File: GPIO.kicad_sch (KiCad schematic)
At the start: 10 parts

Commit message: PCB drawn
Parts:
- C30, C31: value (none) -> 100n; footprint (none) -> Capacitor_SMD:C_0603_1608Metric
- R15: value (none) -> 10K; footprint (none) -> Resistor_SMD:R_0603_1608Metric
- R16, R17: value (none) -> 4.7K; footprint (none) -> Resistor_SMD:R_0603_1608Metric
- R18: value (none) -> 2.2K; footprint (none) -> Resistor_SMD:R_0603_1608Metric
- R19, R20: value (none) -> 68; footprint (none) -> Resistor_SMD:R_0603_1608Metric
- U10: value (none) -> PCF8574; footprint (none) -> EXTRA IC:SOIC127P1032X265-16N
- U9: value (none) -> ATtiny85V-10S; footprint (none) -> Package_SO:SOIC-8W_5.3x5.3mm_P1.27mm
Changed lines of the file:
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@@
   (symbol (lib_id "power:GND") (at 168.91 107.95 0) (unit 1)
     (in_bom yes) (on_board yes) (fields_autoplaced)
-    (property "Reference" "#PWR?" (id 0) (at 168.91 114.3 0)
-      (effects (font (size 1.27 1.27)) hide)
-    )
-    (property "Value" "" (id 1) (at 168.91 112.3934 0))
+    (property "Reference" "#PWR0124" (id 0) (at 168.91 114.3 0)
+      (effects (font (size 1.27 1.27)) hide)
+    )
+    (property "Value" "GND" (id 1) (at 168.91 112.3934 0))
     (property "Footprint" "" (id 2) (at 168.91 107.95 0)
       (effects (font (size 1.27 1.27)) hide)
@@
   (symbol (lib_id "power:GND") (at 182.88 124.46 0) (unit 1)
     (in_bom yes) (on_board yes) (fields_autoplaced)
-    (property "Reference" "#PWR?" (id 0) (at 182.88 130.81 0)
-      (effects (font (size 1.27 1.27)) hide)
-    )
-    (property "Value" "" (id 1) (at 182.88 128.9034 0))
+    (property "Reference" "#PWR0120" (id 0) (at 182.88 130.81 0)
+      (effects (font (size 1.27 1.27)) hide)
+    )
+    (property "Value" "GND" (id 1) (at 182.88 128.9034 0))
     (property "Footprint" "" (id 2) (at 182.88 124.46 0)
       (effects (font (size 1.27 1.27)) hide)
@@
   (symbol (lib_id "power:GND") (at 110.49 120.65 0) (unit 1)
     (in_bom yes) (on_board yes) (fields_autoplaced)
-    (property "Reference" "#PWR?" (id 0) (at 110.49 127 0)
-      (effects (font (size 1.27 1.27)) hide)
-    )
-    (property "Value" "" (id 1) (at 110.49 125.0934 0))
+    (property "Reference" "#PWR0121" (id 0) (at 110.49 127 0)
+      (effects (font (size 1.27 1.27)) hide)
+    )
+    (property "Value" "GND" (id 1) (at 110.49 125.0934 0))
     (property "Footprint" "" (id 2) (at 110.49 120.65 0)
       (effects (font (size 1.27 1.27)) hide)
@@
       (effects (font (size 1.27 1.27)) (justify right))
     )
-    (property "Value" "" (id 1) (at 153.8986 89.3322 0)
-      (effects (font (size 1.27 1.27)) (justify right))
-    )
-    (property "Footprint" "" (id 2) (at 152.4 87.63 0)
+    (property "Value" "10K" (id 1) (at 153.8986 89.3322 0)
+      (effects (font (size 1.27 1.27)) (justify right))
+    )
+    (property "Footprint" "Resistor_SMD:R_0603_1608Metric" (id 2) (at 152.4 87.63 0)
       (effects (font (size 1.27 1.27)) hide)
     )
@@
     (in_bom yes) (on_board yes)
     (property "Reference" "R19" (id 0) (at 133.35 101.6 90))
-    (property "Value" "" (id 1) (at 130.81 100.33 90))
-    (property "Footprint" "" (id 2) (at 130.81 102.87 0)
+    (property "Value" "68" (id 1) (at 130.81 100.33 90))
+    (property "Footprint" "Resistor_SMD:R_0603_1608Metric" (id 2) (at 130.81 102.87 0)
       (effects (font (size 1.27 1.27)) hide)
     )
@@
       (effects (font (size 1.27 1.27)) (justify left))
     )
-    (property "Value" "" (id 1) (at 184.8994 87.7371 0)
-      (effects (font (size 1.27 1.27)) (justify left))
-    )
-    (property "Footprint" "" (id 2) (at 182.88 104.14 0)
+    (property "Value" "PCF8574" (id 1) (at 184.8994 87.7371 0)
+      (effects (font (size 1.27 1.27)) (justify left))
+    )
+    (property "Footprint" "EXTRA IC:SOIC127P1032X265-16N" (id 2) (at 182.88 104.14 0)
       (effects (font (size 1.27 1.27)) hide)
     )
@@
     (in_bom yes) (on_board yes)
     (property "Reference" "R20" (id 0) (at 133.35 104.14 90))
-    (property "Value" "" (id 1) (at 130.81 107.95 90))
-    (property "Footprint" "" (id 2) (at 130.81 105.41 0)
+    (property "Value" "68" (id 1) (at 130.81 107.95 90))
+    (property "Footprint" "Resistor_SMD:R_0603_1608Metric" (id 2) (at 130.81 105.41 0)
       (effects (font (size 1.27 1.27)) hide)
     )
@@
   (symbol (lib_id "power:GND") (at 64.77 101.6 0) (unit 1)
     (in_bom yes) (on_board yes) (fields_autoplaced)
-    (property "Reference" "#PWR?" (id 0) (at 64.77 107.95 0)
-      (effects (font (size 1.27 1.27)) hide)
-    )
-    (property "Value" "" (id 1) (at 64.77 106.0434 0))
+    (property "Reference" "#PWR0122" (id 0) (at 64.77 107.95 0)
+      (effects (font (size 1.27 1.27)) hide)
+    )
+    (property "Value" "GND" (id 1) (at 64.77 106.0434 0))
     (property "Footprint" "" (id 2) (at 64.77 101.6 0)
       (effects (font (size 1.27 1.27)) hide)
@@
       (effects (font (size 1.27 1.27)) (justify right))
     )
-    (property "Value" "" (id 1) (at 138.6586 96.9522 0)
-      (effects (font (size 1.27 1.27)) (justify right))
-    )
-    (property "Footprint" "" (id 2) (at 137.16 95.25 0)
+    (property "Value" "2.2K" (id 1) (at 138.6586 96.9522 0)
+      (effects (font (size 1.27 1.27)) (justify right))
+    )
+    (property "Footprint" "Resistor_SMD:R_0603_1608Metric" (id 2) (at 137.16 95.25 0)
       (effects (font (size 1.27 1.27)) hide)
     )
@@
   (symbol (lib_id "power:GND") (at 73.66 101.6 0) (unit 1)
     (in_bom yes) (on_board yes) (fields_autoplaced)
-    (property "Reference" "#PWR?" (id 0) (at 73.66 107.95 0)
-      (effects (font (size 1.27 1.27)) hide)
-    )
-    (property "Value" "" (id 1) (at 73.66 106.0434 0))
+    (property "Reference" "#PWR0123" (id 0) (at 73.66 107.95 0)
+      (effects (font (size 1.27 1.27)) hide)
+    )
+    (property "Value" "GND" (id 1) (at 73.66 106.0434 0))
     (property "Footprint" "" (id 2) (at 73.66 101.6 0)
       (effects (font (size 1.27 1.27)) hide)
@@
       (effects (font (size 1.27 1.27)) (justify right))
     )
-    (property "Value" "" (id 1) (at 97.0281 104.5722 0)
-      (effects (font (size 1.27 1.27)) (justify right))
-    )
-    (property "Footprint" "" (id 2) (at 110.49 102.87 0)
+    (property "Value" "ATtiny85V-10S" (id 1) (at 97.0281 104.5722 0)
+      (effects (font (size 1.27 1.27)) (justify right))
+    )
+    (property "Footprint" "Package_SO:SOIC-8W_5.3x5.3mm_P1.27mm" (id 2) (at 110.49 102.87 0)
       (effects (font (size 1.27 1.27) italic) hide)
     )
@@
       (effects (font (size 1.27 1.27)) (justify left))
     )
-    (property "Value" "" (id 1) (at 75.9841 98.2285 0)
-      (effects (font (size 1.27 1.27)) (justify left))
-    )
-    (property "Footprint" "" (id 2) (at 73.66 96.52 0)
+    (property "Value" "100n" (id 1) (at 75.9841 98.2285 0)
+      (effects (font (size 1.27 1.27)) (justify left))
+    )
+    (property "Footprint" "Capacitor_SMD:C_0603_1608Metric" (id 2) (at 73.66 96.52 0)
       (effects (font (size 1.27 1.27)) hide)
     )
@@
       (effects (font (size 1.27 1.27)) (justify right))
     )
-    (property "Value" "" (id 1) (at 160.2486 89.3322 0)
-      (effects (font (size 1.27 1.27)) (justify right))
-    )
-    (property "Footprint" "" (id 2) (at 158.75 87.63 0)
+    (property "Value" "4.7K" (id 1) (at 160.2486 89.3322 0)
+      (effects (font (size 1.27 1.27)) (justify right))
+    )
+    (property "Footprint" "Resistor_SMD:R_0603_1608Metric" (id 2) (at 158.75 87.63 0)
       (effects (font (size 1.27 1.27)) hide)
     )
@@
       (effects (font (size 1.27 1.27)) (justify right))
     )
-    (property "Value" "" (id 1) (at 167.8686 89.3322 0)
-      (effects (font (size 1.27 1.27)) (justify right))
-    )
-    (property "Footprint" "" (id 2) (at 166.37 87.63 0)
+    (property "Value" "4.7K" (id 1) (at 167.8686 89.3322 0)
+      (effects (font (size 1.27 1.27)) (justify right))
+    )
+    (property "Footprint" "Resistor_SMD:R_0603_1608Metric" (id 2) (at 166.37 87.63 0)
       (effects (font (size 1.27 1.27)) hide)
     )
@@
       (effects (font (size 1.27 1.27)) (justify left))
     )
-    (property "Value" "" (id 1) (at 67.0941 98.2285 0)
-      (effects (font (size 1.27 1.27)) (justify left))
-    )
-    (property "Footprint" "" (id 2) (at 64.77 96.52 0)
-      (effects (font (size 1.27 1.27)) hide)
-    )
+    (property "Value" "100n" (id 1) (at 67.0941 98.2285 0)
+      (effects (font (size 1.27 1.27)) (justify left))
+    )
+    (property "Footprint" "Capacitor_SMD:C_0603_1608Metric" (id 2) (at 64.77 96.52 0)
+      (effects (font (size 1.27 1.27)) hide)
+    )

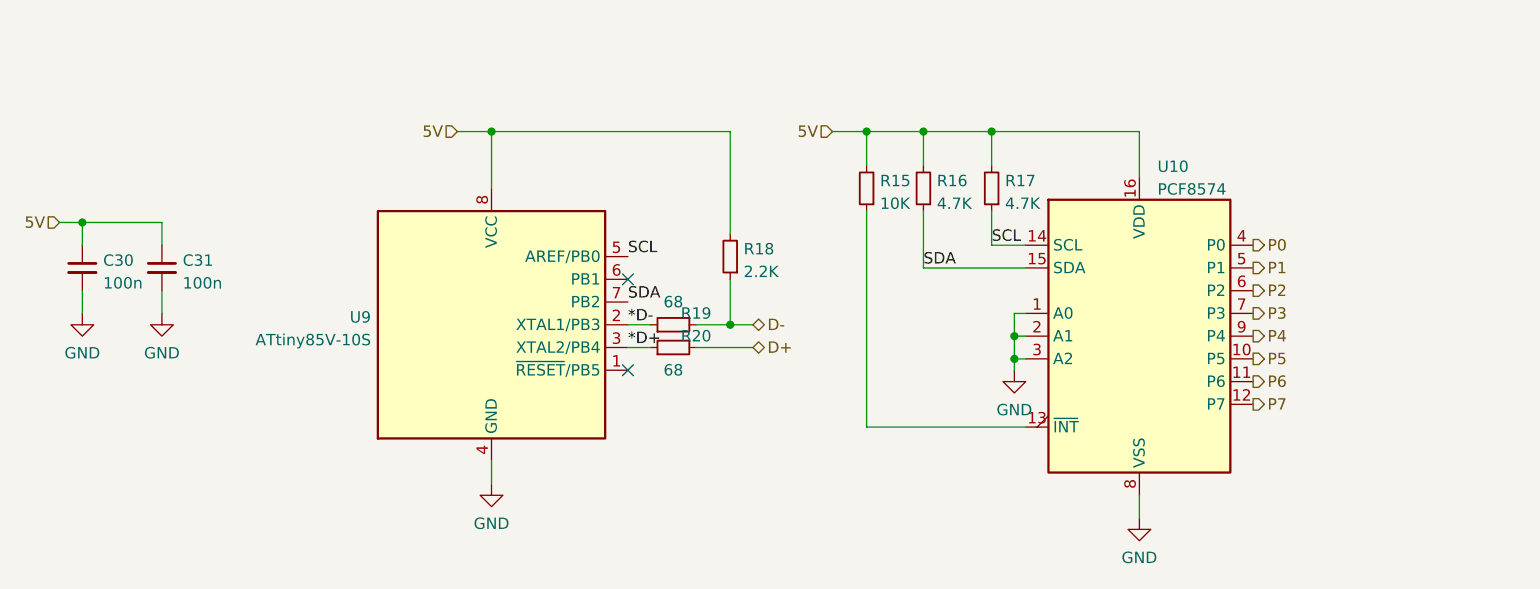
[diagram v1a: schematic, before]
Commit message: Change the map and rebuild the PCB
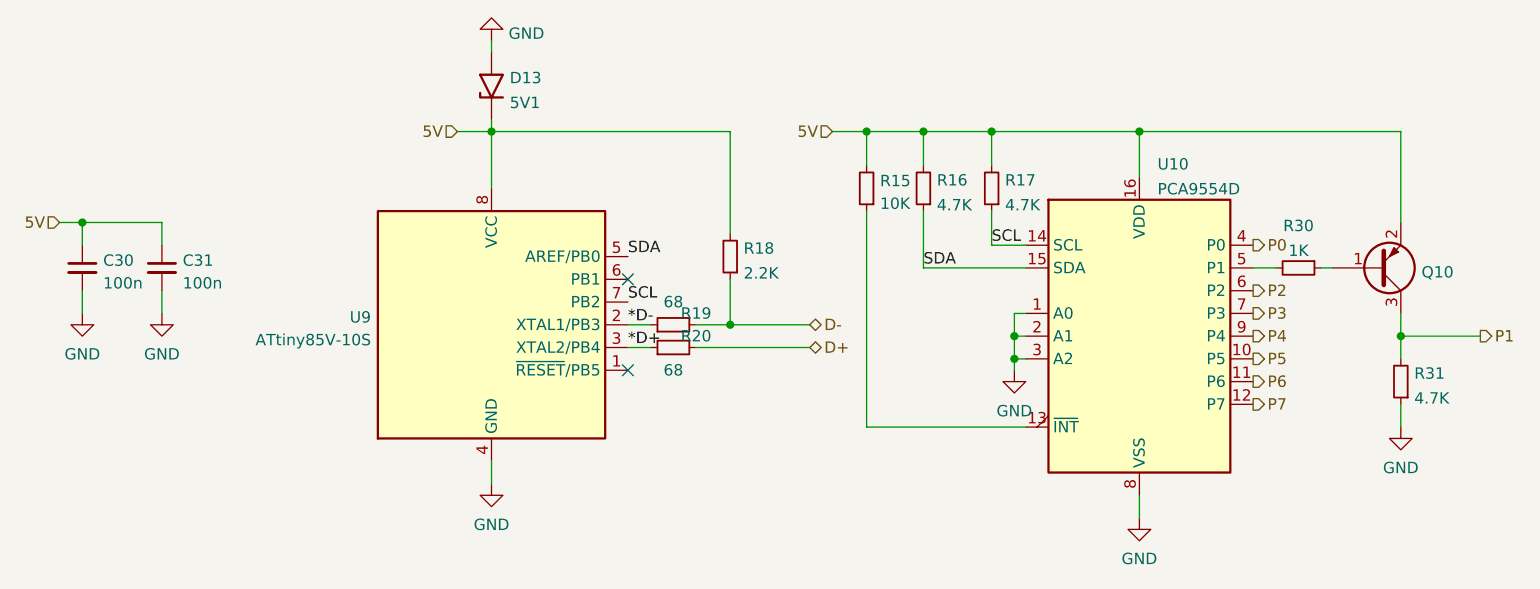
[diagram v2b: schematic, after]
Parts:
- added D13: 5V1, Diode_SMD:D_SOD-123, symbol Diode:1N630xA
- added Q10: Q_PNP_BEC, Package_TO_SOT_SMD:SOT-23, symbol Device:Q_PNP_BEC
- added R30: 1K, Resistor_SMD:R_0603_1608Metric, symbol Device:R_Small
- added R31: 4.7K, Resistor_SMD:R_0603_1608Metric, symbol Device:R_Small
- U10: value PCF8574 -> PCA9554D
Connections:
- net 5V: now also D13.1 (A1), Q10.2 (E)
- net GND: now also D13.2 (A2), R31.1
- net P1: now also Q10.3 (C), R31.2; no longer U10.5 (P1)
- net SCL: now also U9.7 (PB2); no longer U9.5 (AREF/PB0)
- net SDA: now also U9.5 (AREF/PB0); no longer U9.7 (PB2)
- new net: R30.2, U10.5 (P1)
- new net: Q10.1 (B), R30.1
